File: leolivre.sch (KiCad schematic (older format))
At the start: 37 parts

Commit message: pronto para pasar asociar los footprints
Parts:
- removed C?: CP1, symbol CP1
- removed C?: C, symbol C
- removed D?: DIODE, symbol DIODE
- removed J?: RJ45, symbol RJ45
- removed R?: R, symbol R
- removed X?: CRYSTAL, symbol CRYSTAL
- added D2: green, symbol LED
- added P2: ICSP, symbol CONN_4X2
- added P3: PUERTOS IO, symbol CONN_6
- added R12: 1k, symbol R
- C1, C5, C8: renamed from C?; value C -> 0.1uF
- C2: renamed from C?; value CP1 -> 10uF
- C3, C4: renamed from C?; value C -> 22pF
- C6, C7: renamed from C?; value C -> 1uF
- F1: renamed from F?; value FUSE -> 500mA
- J1: renamed from J?; value RJ45 -> Puerto 4
- J3: renamed from J?; value RJ45 -> Puerto 3
- J4: renamed from J?; value RJ45 -> Puerto 2
- J5: renamed from J?; value RJ45 -> Puerto 1
- K1: renamed from K?; value CONN_3 -> AX-12
- L1: renamed from L?; value INDUCTOR -> MH2029-300Y
- R1, R11, R2, R3, R8, R9: renamed from R?; value R -> 10k
- R10: renamed from R?; value R -> 100
- R4: renamed from R?; value R -> 1M
- R5, R6: renamed from R?; value R -> 22
- R7: renamed from R?; value R -> 1k
- SW1: renamed from SW?; value SW_PUSH -> reset
- X1: renamed from X?; value CRYSTAL -> 16Mhz
- gave numbers to parts that had none: 3
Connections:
- net labels added: MISO, MOSI, SCLK, SS
- wire segments 105 -> 125
- no-connect marks 18 -> 28
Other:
- note added: "ICSP"
- note added: "LEOLIVRE"
- note added: "POWER LED"

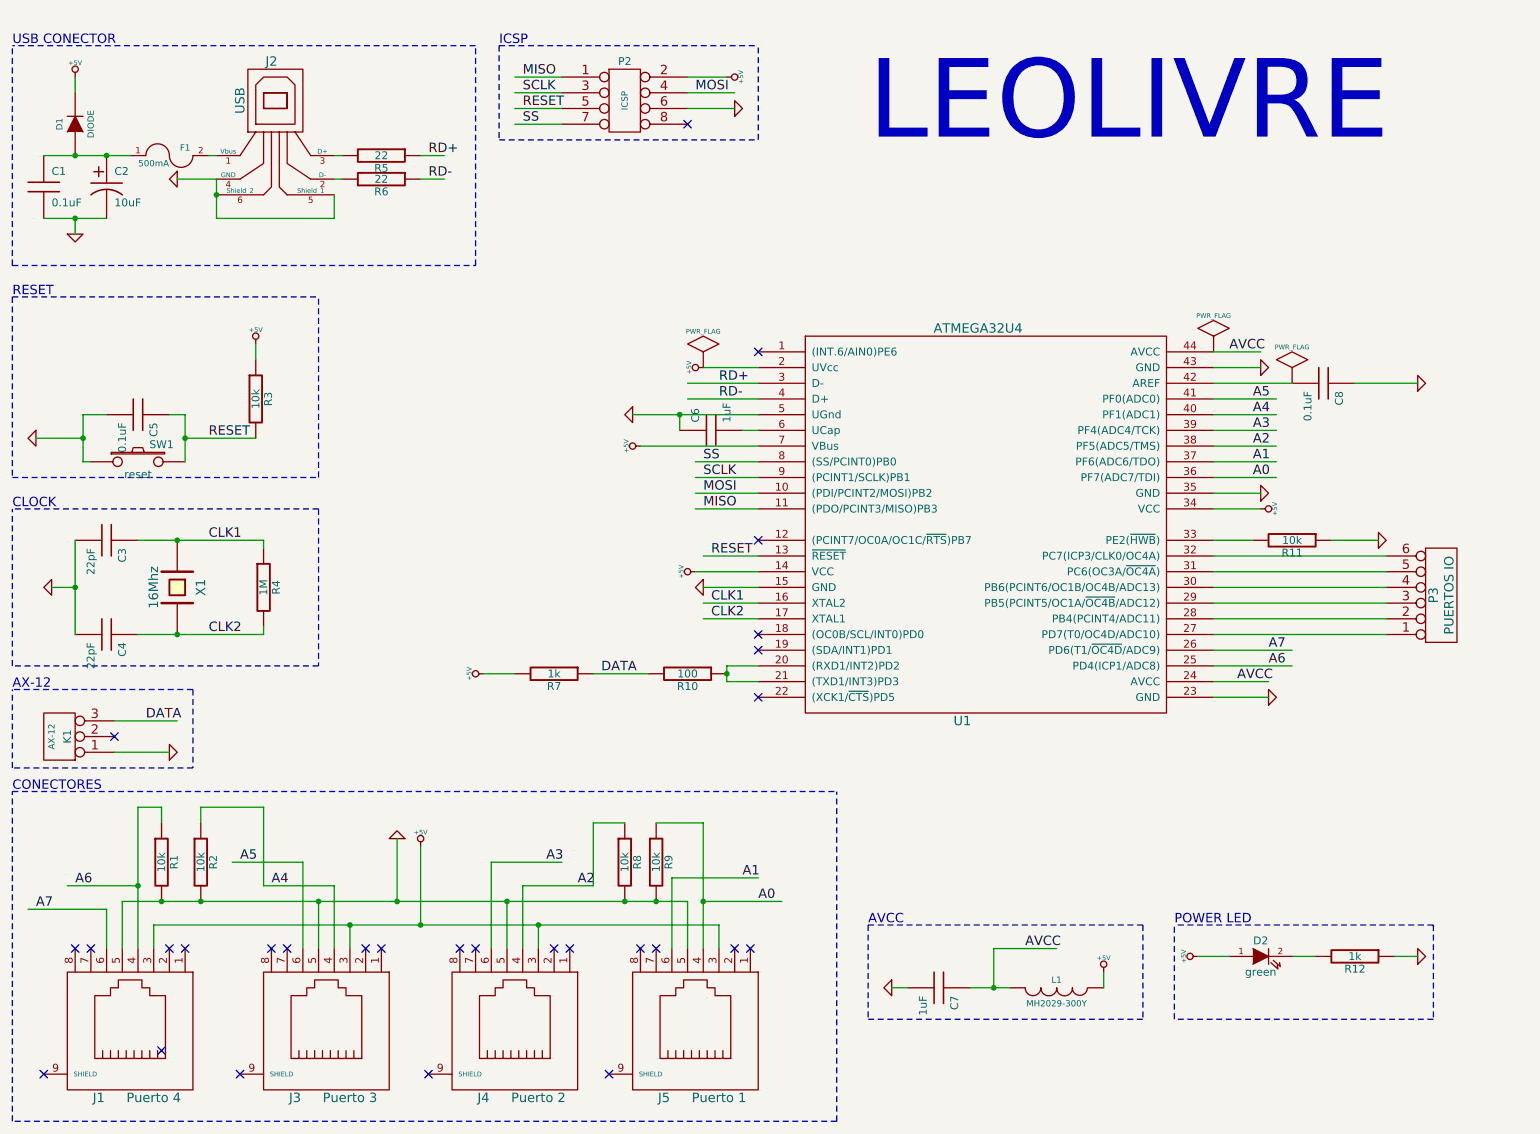
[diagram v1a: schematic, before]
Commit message: mejoras en el grosor de las pistas el isolamento y tamano de las vias
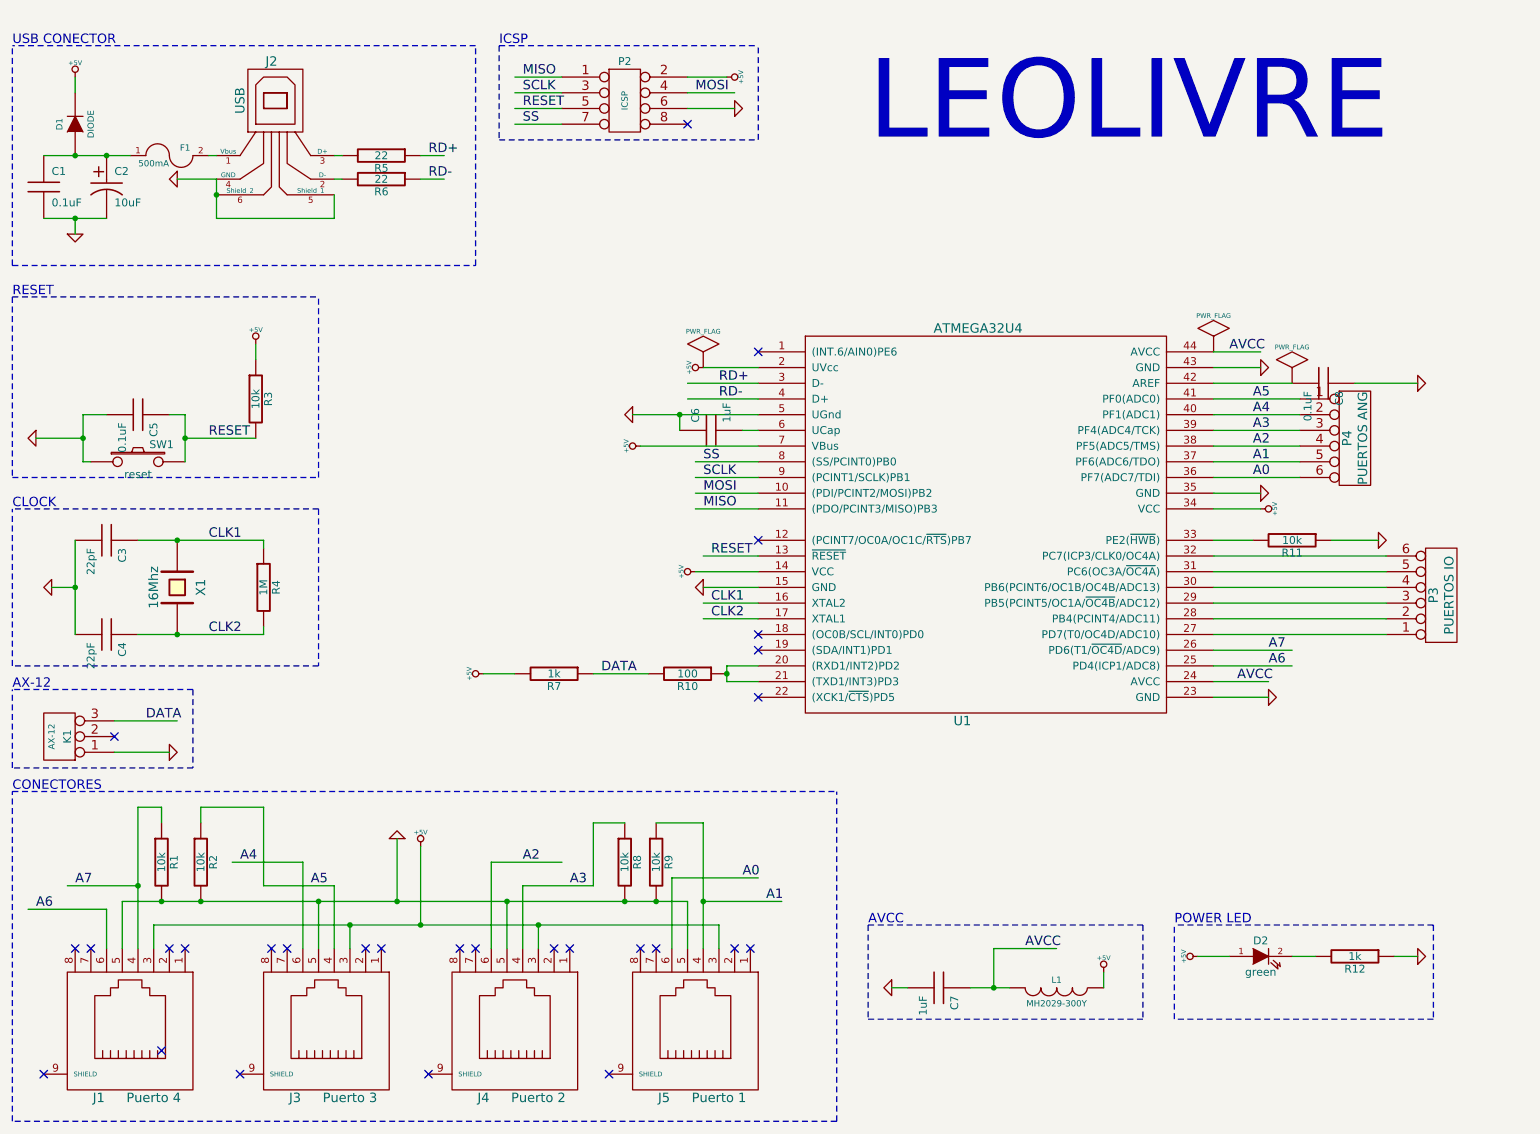
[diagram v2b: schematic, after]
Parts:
- added P4: PUERTOS ANG, symbol CONN_6
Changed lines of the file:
@@
-EESchema Schematic File Version 2  date Sex 15 Mar 2013 14:44:02 BRT
+EESchema Schematic File Version 2  date Sáb 16 Mar 2013 04:15:28 BRT
 LIBS:power
 LIBS:device
@@
 Sheet 1 1
 Title "leolivre"
-Date "15 mar 2013"
-Rev "1.0"
+Date "16 mar 2013"
+Rev "1.1"
 Comp ""
 Comment1 ""
@@
 Comment4 ""
 $EndDescr
-NoConn ~ 5000 1350
+Wire Wire Line
+	8900 3600 8350 3600
+Wire Wire Line
+	8900 3400 8350 3400
+Wire Wire Line
+	8900 3200 8350 3200
 Wire Wire Line
 	4200 1350 3900 1350
@@
 	8350 4700 8850 4700
 Wire Wire Line
-	8350 3100 8750 3100
-Wire Wire Line
-	8350 3300 8750 3300
-Wire Wire Line
-	8350 3500 8750 3500
-Wire Wire Line
 	8350 3700 8650 3700
 Wire Wire Line
@@
 	9250 3000 9650 3000
 Wire Wire Line
-	8350 3600 8750 3600
-Wire Wire Line
-	8350 3400 8750 3400
-Wire Wire Line
-	8350 3200 8750 3200
-Wire Wire Line
 	8350 4800 8850 4800
 Wire Wire Line
@@
 Wire Notes Line
 	5450 1450 5450 850
+Wire Wire Line
+	8900 3100 8350 3100
+Wire Wire Line
+	8900 3300 8350 3300
+Wire Wire Line
+	8900 3500 8350 3500
+$Comp
+L CONN_6 P4
+U 1 1 5143D86F
+P 9250 3350
+F 0 "P4" V 9200 3350 60  0000 C CNN
+F 1 "PUERTOS ANG" V 9300 3350 60  0000 C CNN
+	1    9250 3350
+	1    0    0    -1
+$EndComp
+Text Label 5350 6150 0    60   ~ 0
+A0
+Text Label 5500 6300 0    60   ~ 0
+A1
+NoConn ~ 5000 1350
 $Comp
 L CONN_4X2 P2
@@
 	1    0    0    -1
 $EndComp
+Text Label 1100 6200 0    60   ~ 0
+A7
 Text Label 850  6350 0    60   ~ 0
-A7
-Text Label 1100 6200 0    60   ~ 0
 A6
+Text Label 2600 6200 0    60   ~ 0
+A5
 Text Label 2150 6050 0    60   ~ 0
-A5
-Text Label 2350 6200 0    60   ~ 0
 A4
-Text Label 4100 6050 0    60   ~ 0
+Text Label 4250 6200 0    60   ~ 0
 A3
-Text Label 4300 6200 0    60   ~ 0
+Text Label 3950 6050 0    60   ~ 0
 A2
-Text Label 5350 6150 0    60   ~ 0
-A1
-Text Label 5450 6300 0    60   ~ 0
-A0
 $Comp
 L GND #PWR015
